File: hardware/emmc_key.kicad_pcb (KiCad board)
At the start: 4 copper layers, 16.8 x 30 mm, 7 parts, among them U1 EMMC Module

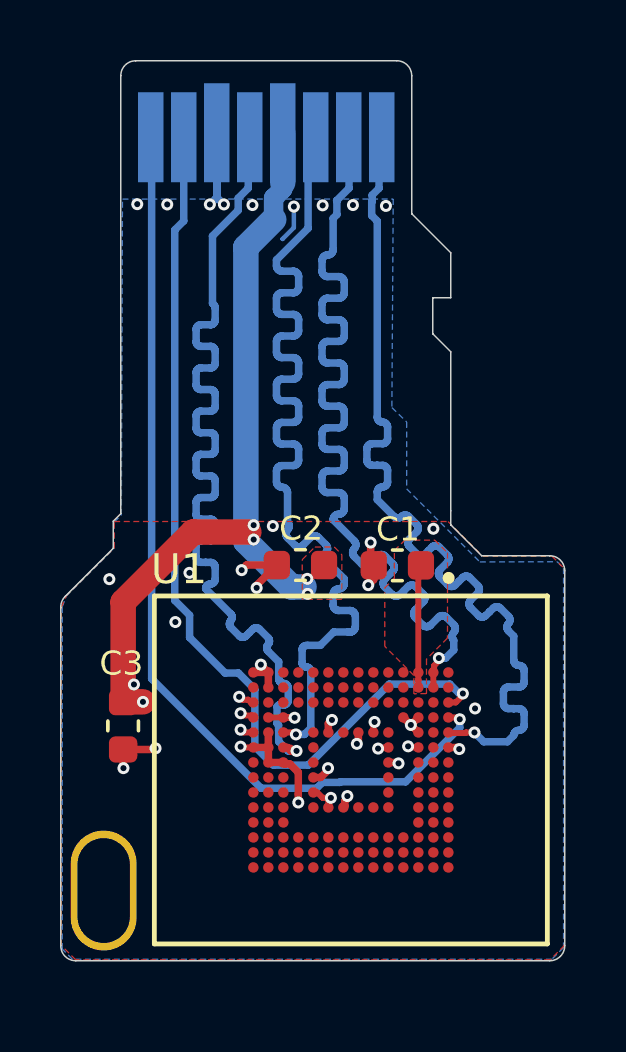
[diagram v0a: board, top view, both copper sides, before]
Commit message: RST_N connected to 3V3. Fabrication outputs regenerated.
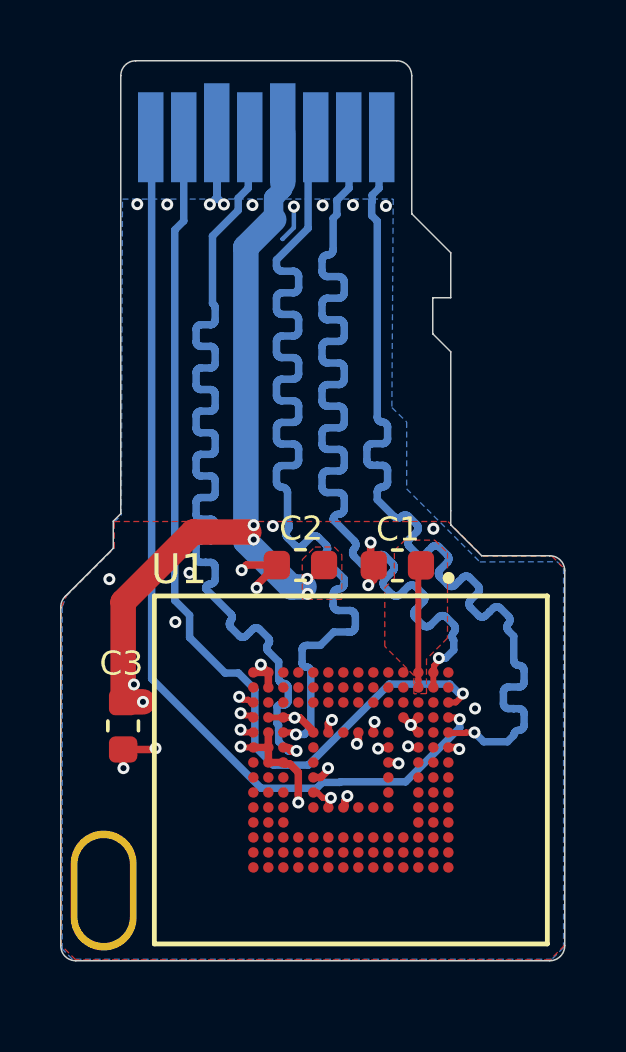
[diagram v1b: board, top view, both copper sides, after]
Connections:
- U1 pad K5: Net-(U1-PadK5) -> +3V3
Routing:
- net +3V3: track 31.5 -> 32.4 mm

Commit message: New variant with voltage translator and 1V8 LDO for eMMC modules where VCCQ is 1V8.
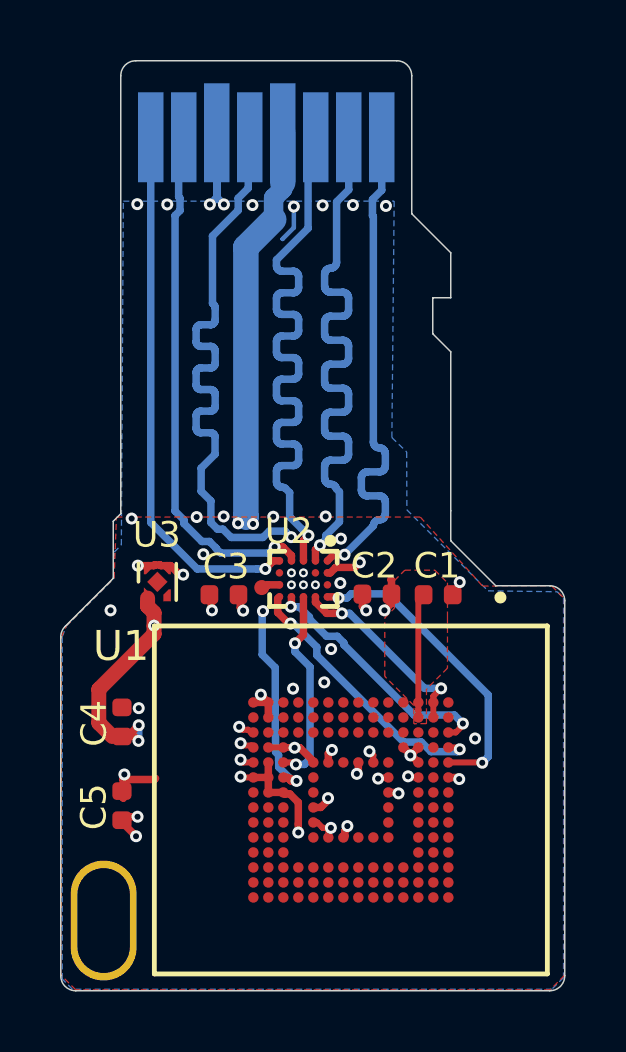
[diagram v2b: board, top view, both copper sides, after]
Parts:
- added C2: 2.2uF, Capacitor_SMD:C_0402_1005Metric, F.Cu at (108.5, 117.8)
- added C4: 2.2uF, Capacitor_SMD:C_0402_1005Metric, F.Cu at (100.0, 122.0)
- added TP1: TestPoint, TestPoint:TestPoint_Pad_D1.0mm, F.Cu at (104.7, 117.6)
- added U2: TXS0206, emmc_key:BGA20N40P5X4_195X155X50N, F.Cu at (106.1, 117.3)
- added U3: LDO 1V8, Package_DFN_QFN:UDFN-4-1EP_1x1mm_P0.65mm_EP0.48x0.48mm, F.Cu at (101.2, 117.4)
- C1, C3: footprint Capacitor_SMD:C_0603_1608Metric -> Capacitor_SMD:C_0402_1005Metric
- C5: renamed from C2; footprint Capacitor_SMD:C_0603_1608Metric -> Capacitor_SMD:C_0402_1005Metric
- moved C5 9.99 mm to (100.0, 124.8), turned to 90 degrees
- moved C3 5.51 mm to (103.4, 117.8), turned to 180 degrees
- moved C1 1.68 mm to (110.6, 117.8), turned to 0 degrees
- moved H1 1.00 mm to (99.5, 129.7)
- moved U1 1.00 mm to (107.7, 124.6)
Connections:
- B1 pad 1: /DAT2 -> /DAT2_CN
- B1 pad 2: /DAT3 -> /DAT3_CN
- B1 pad 3: /CMD -> /CMD_CN
- B1 pad 5: /CLK -> /CLK_CN
- B1 pad 7: /DAT0 -> /DAT0_CN
- B1 pad 8: /DAT1 -> /DAT1_CN
- U1 pad C6: +3V3 -> +1V8
- U1 pad K5: +3V3 -> +1V8
- U1 pad M4: +3V3 -> +1V8
- U1 pad N4: +3V3 -> +1V8
- U1 pad P3: +3V3 -> +1V8
- U1 pad P5: +3V3 -> +1V8
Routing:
- net /CMD: track 31.4 -> 6.72 mm, vias 1 -> 2
- net /DAT3: track 30.8 -> 6.63 mm, vias 1 -> 2
- net /DAT0: track 30.9 -> 8.41 mm, vias 1 -> 2
- net /CLK: track 30.6 -> 8.30 mm, vias 1 -> 3
- net /DAT1: track 31.4 -> 9.13 mm, vias 1 -> 2
- net /CMD_CN: track 0.00 -> 21.0 mm, vias 0 -> 1
- net /CLK_CN: track 0.00 -> 20.9 mm, vias 0 -> 2
- net /DAT2: track 31.0 -> 10.4 mm, vias 1 -> 2
- net /DAT3_CN: track 0.00 -> 20.1 mm, vias 0 -> 1
- net /DAT1_CN: track 0.00 -> 18.0 mm, vias 0 -> 1
- net /DAT0_CN: track 0.00 -> 17.5 mm, vias 0 -> 1
- net /DAT2_CN: track 0.00 -> 16.8 mm, vias 0 -> 1
- net +1V8: track 0.00 -> 13.0 mm, vias 0 -> 9
- net +3V3: track 32.4 -> 19.7 mm, vias 13 -> 11
- net GND: track 21.4 -> 19.3 mm, vias 32 -> 40
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- added copper zone on In1.Cu, net +1V8
- removed copper zone on F.Cu, net +3V3
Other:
- board size 16.8 x 30 mm -> 16.8 x 31 mm
- net class Default: clearance 0.15 -> 0.1
- rule trace_clearance: 0.15 -> 0.1
- rule trace_min: 0.15 -> 0.125
- board text added: "Rev: 1.1"
- board text removed: "Rev: 1.0"

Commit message: Changed 0.15 vias from blind to TH.
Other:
- rule via_min_drill: 0.2 -> 0.15
- rule via_min_size: 0.4 -> 0.3
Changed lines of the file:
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@@
     (via_size 0.4)
     (via_drill 0.2)
-    (via_min_size 0.4)
-    (via_min_drill 0.2)
+    (via_min_size 0.3)
+    (via_min_drill 0.15)
     (uvia_size 0.3)
     (uvia_drill 0.15)
@@
       (padsonsilk false)
       (subtractmaskfromsilk false)
-      (outputformat 4)
+      (outputformat 1)
       (mirror false)
       (drillshape 0)
       (scaleselection 1)
-      (outputdirectory "Outputs/"))
+      (outputdirectory "Outputs/gerbers"))
   )
   (net 0 "")
@@
   (segment (start 106.984988 117.07) (end 107.164988 116.89) (width 0.25) (layer F.Cu) (net 4))
   (segment (start 106.89 117.07) (end 106.984988 117.07) (width 0.25) (layer F.Cu) (net 4))
-  (via micro (at 105.69 117.47) (size 0.3) (drill 0.15) (layers F.Cu In1.Cu) (net 5))
+  (via (at 105.69 117.47) (size 0.3) (drill 0.15) (layers F.Cu B.Cu) (net 5))
   (via (at 105.859774 124.00499) (size 0.4) (drill 0.2) (layers F.Cu B.Cu) (net 5))
   (segment (start 105.77499 124.00499) (end 105.859774 124.00499) (width 0.2) (layer F.Cu) (net 5))
@@
   (via (at 107.34 115.93) (size 0.4) (drill 0.2) (layers F.Cu B.Cu) (net 6))
   (via (at 107.32 117.41) (size 0.4) (drill 0.2) (layers F.Cu B.Cu) (net 6))
-  (via micro (at 106.09 117.47) (size 0.3) (drill 0.15) (layers F.Cu In1.Cu) (net 6))
-  (via micro (at 106.09 117.07) (size 0.3) (drill 0.15) (layers F.Cu In1.Cu) (net 6))
+  (via (at 106.09 117.47) (size 0.3) (drill 0.15) (layers F.Cu B.Cu) (net 6))
+  (via (at 106.09 117.07) (size 0.3) (drill 0.15) (layers F.Cu B.Cu) (net 6))
   (via (at 103.04 118.32) (size 0.4) (drill 0.2) (layers F.Cu B.Cu) (net 6))
   (via (at 111.3 117.38) (size 0.4) (drill 0.2) (layers F.Cu B.Cu) (net 6))
@@
   (segment (start 105.19 110.8) (end 105.19 111.15) (width 0.25) (layer B.Cu) (net 22))
   (segment (start 105.860346 109.134638) (end 105.825269 109.156679) (width 0.25) (layer B.Cu) (net 22))
-  (via micro (at 105.69 117.07) (size 0.3) (drill 0.15) (layers F.Cu In1.Cu) (net 23))
+  (via (at 105.69 117.07) (size 0.3) (drill 0.15) (layers F.Cu B.Cu) (net 23))
   (segment (start 105.480058 115.679381) (end 105.680057 115.87938) (width 0.25) (layer B.Cu) (net 23))
   (segment (start 104.951615 115.679381) (end 105.480058 115.679381) (width 0.25) (layer B.Cu) (net 23))
@@
   (via (at 101.11 118.83) (size 0.4) (drill 0.2) (layers F.Cu B.Cu) (net 26))
   (segment (start 101.11 118.86) (end 101.11 118.83) (width 0.25) (layer F.Cu) (net 26))
-  (via micro (at 106.49 117.47) (size 0.3) (drill 0.15) (layers F.Cu In1.Cu) (net 26))
+  (via (at 106.49 117.47) (size 0.3) (drill 0.15) (layers F.Cu B.Cu) (net 26))
   (segment (start 106.49 117.47) (end 106.49 118.07) (width 0.25) (layer In1.Cu) (net 26))
   (via (at 100.6 122.15) (size 0.4) (drill 0.2) (layers F.Cu B.Cu) (net 26))
